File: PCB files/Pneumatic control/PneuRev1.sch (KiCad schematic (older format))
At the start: 53 parts, among them J1 SIG_IN, J2 BATT_IN, J3 PNEU, U1 uA7824, U2 OP279, U3 OP279, U4 OP279, U5 OP279, U6 OP279, U7 OP279, U8 OP07

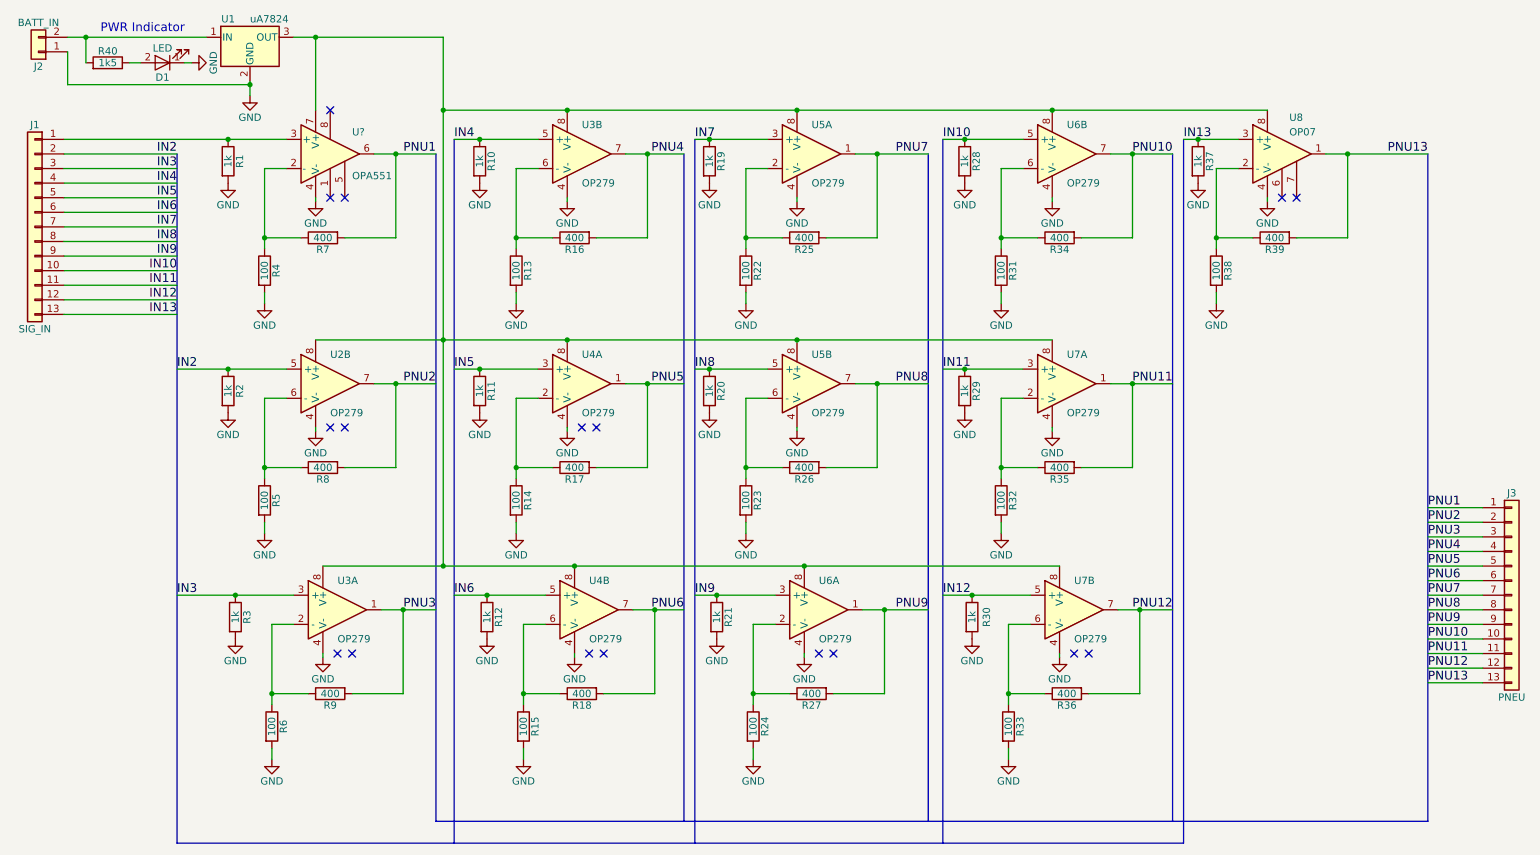
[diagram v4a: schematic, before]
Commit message: 2/15/2019
Schematic edits
-replaced old opamp with OPA551
-removed ua24 regulator
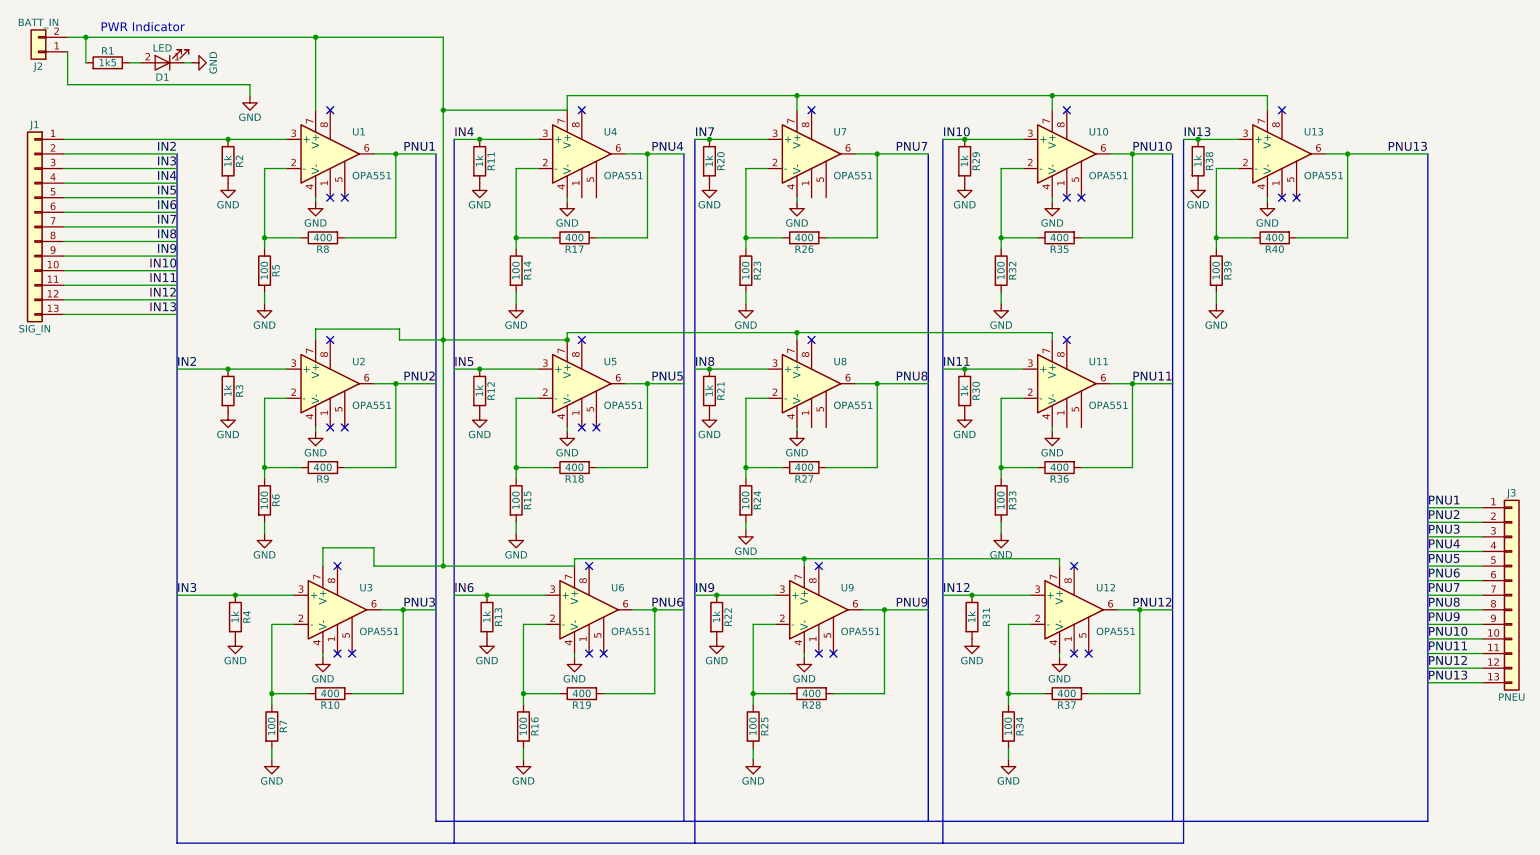
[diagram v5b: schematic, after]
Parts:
- removed U1: uA7824, ua7824:TO254P1651X1067X470-3, symbol uA7824
- removed U2, U3, U4, U5, U6, U7: OP279, dualopamp:SOIC127P600X175-8N, symbol OP279
- removed U8: OP07, dualopamp:SOIC127P600X175-8N, symbol OP07
- added U10, U11, U12, U13, U2, U3, U4, U5, U6, U7, U8, U9: OPA551, symbol OPA551
- gave numbers to parts that had none: 1
- renumbered R40 to R1, R9 to R10, R10 to R11, R11 to R12, R12 to R13, R13 to R14, R14 to R15, R15 to R16, R16 to R17, R17 to R18, R18 to R19, R1 to R2, R19 to R20, R20 to R21, R21 to R22, R22 to R23, R23 to R24, R24 to R25, R25 to R26, R26 to R27, R27 to R28, R28 to R29, R2 to R3, R29 to R30, R30 to R31, R31 to R32, R32 to R33, R33 to R34, R34 to R35, R35 to R36, R36 to R37, R37 to R38, R38 to R39, R3 to R4, R39 to R40, R4 to R5, R5 to R6, R6 to R7, R7 to R8, R8 to R9
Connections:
- net GND: now also U10.4 (V-), U11.4 (V-), U12.4 (V-), U13.4 (V-), U2.4 (V-), U3.4 (V-), U4.4 (V-), U5.4 (V-), U6.4 (V-), U7.4 (V-), U8.4 (V-), U9.4 (V-)
- net IN10: now also U10.3 (+)
- net IN11: now also U11.3 (+)
- net IN12: now also U12.3 (+)
- net IN13: now also U13.3 (+)
- net IN2: now also U2.3 (+)
- net IN3: now also U3.3 (+)
- net IN4: now also U4.3 (+)
- net IN5: now also U5.3 (+)
- net IN6: now also U6.3 (+)
- net IN7: now also U7.3 (+)
- net IN8: now also U8.3 (+)
- net IN9: now also U9.3 (+)
- net PNU10: now also U10.6
- net PNU11: now also U11.6
- net PNU12: now also U12.6
- net PNU13: now also U13.6
- net PNU2: now also U2.6
- net PNU3: now also U3.6
- net PNU4: now also U4.6
- net PNU5: now also U5.6
- net PNU6: now also U6.6
- net PNU7: now also U7.6
- net PNU8: now also U8.6
- net PNU9: now also U9.6
- net at J2.2 (Pin_2), R1.2: now also U1.7 (V+), U10.7 (V+), U11.7 (V+), U12.7 (V+), U13.7 (V+), U2.7 (V+), U3.7 (V+), U4.7 (V+), U5.7 (V+), U6.7 (V+), U7.7 (V+), U8.7 (V+), U9.7 (V+)
- net at R6.1, R9.1: now also U2.2 (-)
- net at R10.1, R7.1: now also U3.2 (-)
- net at R14.1, R17.1: now also U4.2 (-)
- net at R15.1, R18.1: now also U5.2 (-)
- net at R16.1, R19.1: now also U6.2 (-)
- net at R23.1, R26.1: now also U7.2 (-)
- net at R24.1, R27.1: now also U8.2 (-)
- net at R25.1, R28.1: now also U9.2 (-)
- net at R32.1, R35.1: now also U10.2 (-)
- net at R33.1, R36.1: now also U11.2 (-)
- net at R34.1, R37.1: now also U12.2 (-)
- net at R39.1, R40.1: now also U13.2 (-)
- no-connect marks 17 -> 31

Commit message: 2/15/2019
-Updated schematic symbols
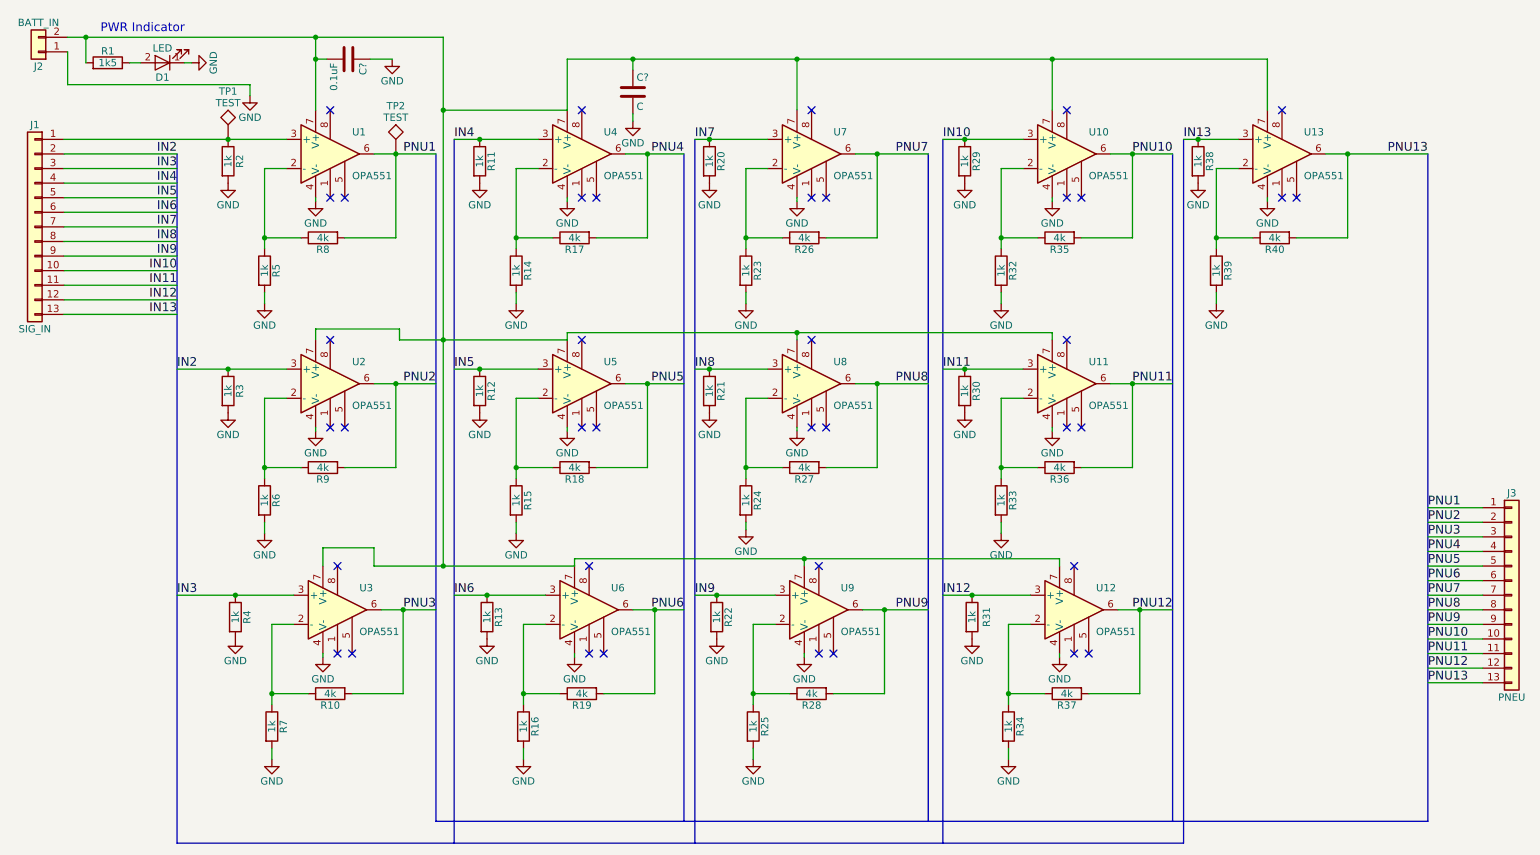
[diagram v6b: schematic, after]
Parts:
- added C?: 0.1uF, symbol C
- added C?: C, symbol C
- added TP1, TP2: TEST, Measurement_Points:Measurement_Point_Round-SMD-Pad_Big, symbol TEST
- R10, R17, R18, R19, R26, R27, R28, R35, R36, R37, R8, R9: value 400 -> 4k
- R14, R15, R16, R23, R24, R25, R32, R33, R34, R39, R5, R6, R7: value 100 -> 1k; footprint Resistors_THT:R_Axial_DIN0204_L3.6mm_D1.6mm_P7.62mm_Horizontal -> Resistors_THT:R_Axial_DIN0204_L3.6mm_D1.6mm_P5.08mm_Horizontal
- R40: value 400 -> 4k; footprint Resistors_THT:R_Axial_DIN0411_L9.9mm_D3.6mm_P12.70mm_Horizontal -> Resistors_THT:R_Axial_DIN0204_L3.6mm_D1.6mm_P5.08mm_Horizontal
- U1, U10, U11, U12, U13, U2, U3, U4, U5, U6, U7, U8, U9: footprint (none) -> Housings_DIP:DIP-8_W7.62mm
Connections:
- net GND: now also C?.1, C?.2
- net PNU1: now also TP2.1
- net at J1.1 (Pin_1), R2.1, U1.3 (+): now also TP1.1
- net at J2.2 (Pin_2), R1.2, U1.7 (V+)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: now also C?.1, C?.2
- no-connect marks 31 -> 39

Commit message: 2/19/2019
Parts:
- removed C?: C, symbol C
- added C10, C11, C12, C13, C2, C3, C4, C5, C6, C7, C8, C9: 1uF, symbol C
- C1: renamed from C?; value 0.1uF -> 1uF
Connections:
- net GND: now also C10.1, C11.1, C12.1, C13.1, C2.1, C3.1, C4.1, C5.1, C6.1, C7.1, C8.1, C9.1
- net at C1.2, J2.2 (Pin_2), R1.2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: now also C10.2, C11.2, C12.2, C13.2, C2.2, C3.2, C4.2, C5.2, C6.2, C7.2, C8.2, C9.2

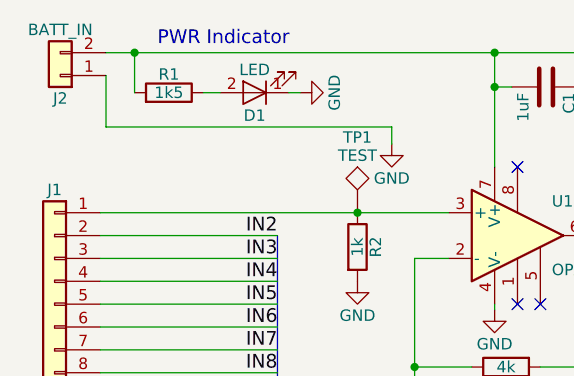
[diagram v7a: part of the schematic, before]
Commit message: 2/21/2019
-Selected capacitor footprint
-Generated netlist
-Began re-routing board
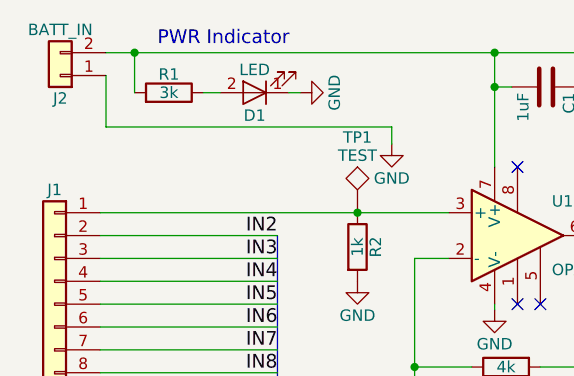
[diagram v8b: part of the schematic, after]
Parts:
- C1, C10, C11, C12, C13, C2, C3, C4, C5, C6, C7, C8, C9: footprint (none) -> Capacitors_THT:C_Disc_D3.4mm_W2.1mm_P2.50mm
- R1: value 1k5 -> 3k
